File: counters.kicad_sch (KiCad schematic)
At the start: 21 parts, among them J10 Conn_01x10_Socket, J11 Conn_01x06_Socket, J12 Conn_01x10_Socket, J13 Conn_01x03_Socket, J8 Conn_01x10_Socket, J9 Conn_01x06_Socket, SW1 SW_Push, SW2 SW_Push

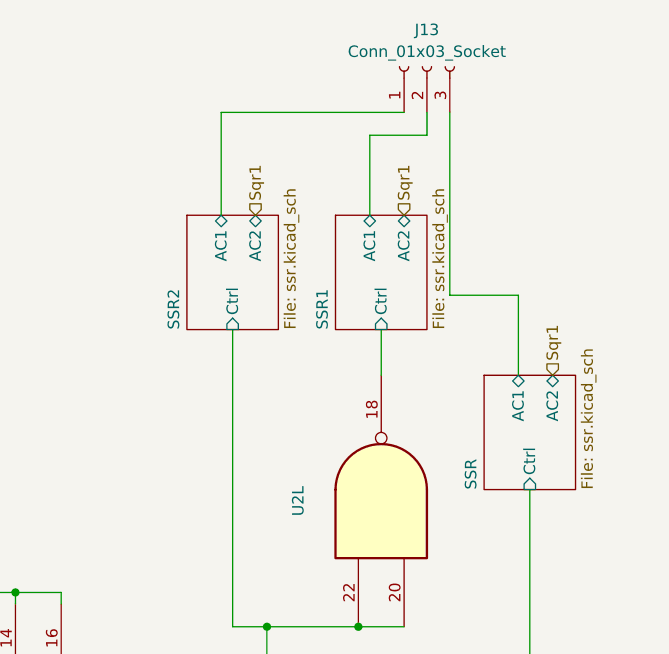
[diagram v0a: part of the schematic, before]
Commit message: switched to using SSR module
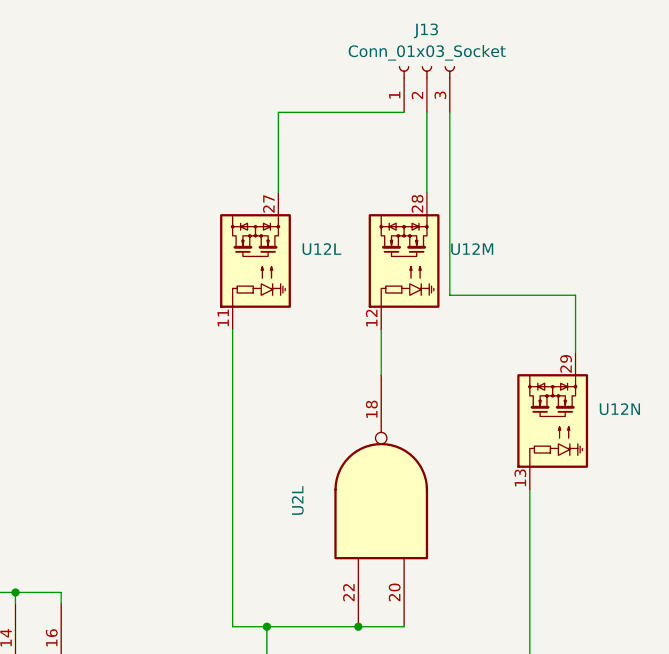
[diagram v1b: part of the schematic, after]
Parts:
- added U12: ~, symbol custom:SSR
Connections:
- net BCD_h1/Q0: now also U12.11
- net BCD_h1/Q1: now also U12.13
- net SSR/AC1: no longer names the net of J13.3 (Pin_3)
- net SSR/AC1: now also U12.29
- net SSR1/AC1: no longer names the net of J13.2 (Pin_2)
- net SSR1/AC1: now also U12.28
- net SSR1/Ctrl: no longer names the net of U2.18
- net SSR1/Ctrl: now also U12.12
- net SSR2/AC1: no longer names the net of J13.1 (Pin_1)
- net SSR2/AC1: now also U12.27
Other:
- removed sheet SSR
- removed sheet SSR1
- removed sheet SSR2

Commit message: added LCSC part numbers
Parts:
- C30, C31, C32, C33, C34, C35, C36: LCSC Part # (none) -> C57112
- R13, R15: LCSC Part # (none) -> C25804
- R14, R16: LCSC Part # (none) -> C21190
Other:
- sheet relays_m1 ports: added none; removed Sqr1
- sheet relays_s1 ports: added none; removed Sqr1

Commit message: switched clock to bjt astable multivibrator
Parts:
- U1: now not fitted
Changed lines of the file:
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@@
 		(in_bom yes)
 		(on_board yes)
-		(dnp no)
+		(dnp yes)
 		(property "Reference" "U1"
 			(at 217.678 113.538 90)
@@
 		(in_bom yes)
 		(on_board yes)
-		(dnp no)
+		(dnp yes)
 		(property "Reference" "U1"
 			(at 51.816 114.1617 90)
@@
 		(in_bom yes)
 		(on_board yes)
-		(dnp no)
+		(dnp yes)
 		(property "Reference" "U1"
 			(at 135.128 114.1617 90)

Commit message: changed some components to lcsc parts
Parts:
- U1: now fitted
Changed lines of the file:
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@@
 		(in_bom yes)
 		(on_board yes)
-		(dnp yes)
+		(dnp no)
 		(property "Reference" "U1"
 			(at 217.678 113.538 90)
@@
 		(in_bom yes)
 		(on_board yes)
-		(dnp yes)
+		(dnp no)
 		(property "Reference" "U1"
 			(at 51.816 114.1617 90)
@@
 		(in_bom yes)
 		(on_board yes)
-		(dnp yes)
+		(dnp no)
 		(property "Reference" "U1"
 			(at 135.128 114.1617 90)

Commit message: added footprints for modules
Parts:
- U14: renamed from U1; footprint (none) -> custom:module_bdc_mpcie
- U15: renamed from U2; footprint (none) -> custom:module_bdc_mpcie
- U9: renamed from U12; footprint (none) -> custom:module_ssr
- renumbered C30 to C16, C31 to C17, C32 to C18, C33 to C19, C34 to C20, C35 to C21, C36 to C22

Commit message: added module for PSU
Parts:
- U3: renamed from U9; value ~ -> SSR
- U8: renamed from U14; value ~ -> bin-to-dec; LCSC Part # (none) -> C185937
- U9: renamed from U15; value ~ -> bin-to-dec; LCSC Part # (none) -> C185937
- renumbered R13 to R14, R14 to R15, R15 to R16, R16 to R17
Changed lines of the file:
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@@
 		(on_board yes)
 		(dnp no)
-		(property "Reference" "U14"
+		(property "Reference" "U8"
 			(at 217.678 113.538 90)
 			(effects
@@
 			)
 		)
-		(property "Value" "~"
+		(property "Value" "bin-to-dec"
 			(at 219.202 115.316 90)
 			(effects
@@
 			)
 		)
-		(property "LCSC Part #" ""
+		(property "LCSC Part #" "C185937"
 			(at 228.6 96.52 90)
 			(effects
@@
 			(project "transistor-clock"
 				(path "/ce10d5bc-995e-4952-aa76-0a08f713a0f2/2c36a9e9-de42-4705-9ad4-94f4cc168e2f"
-					(reference "U14")
+					(reference "U8")
 					(unit 13)
 				)
@@
 		(dnp no)
 		(fields_autoplaced yes)
-		(property "Reference" "U9"
+		(property "Reference" "U3"
 			(at 281.432 78.7978 90)
 			(effects
@@
 			)
 		)
-		(property "Value" "~"
+		(property "Value" "SSR"
 			(at 281.432 81.2221 90)
 			(effects
@@
 			(project "transistor-clock"
 				(path "/ce10d5bc-995e-4952-aa76-0a08f713a0f2/2c36a9e9-de42-4705-9ad4-94f4cc168e2f"
-					(reference "U9")
+					(reference "U3")
 					(unit 14)
 				)
@@
 		(dnp no)
 		(fields_autoplaced yes)
-		(property "Reference" "U15"
+		(property "Reference" "U9"
 			(at 76.189 133.0155 0)
 			(effects
@@
 			)
 		)
-		(property "Value" "~"
+		(property "Value" "bin-to-dec"
 			(at 76.189 135.4398 0)
 			(effects
@@
 			)
 		)
-		(property "LCSC Part #" ""
+		(property "LCSC Part #" "C185937"
 			(at 63.5 135.89 0)
 			(effects
@@
 			(project "transistor-clock"
 				(path "/ce10d5bc-995e-4952-aa76-0a08f713a0f2/2c36a9e9-de42-4705-9ad4-94f4cc168e2f"
-					(reference "U15")
+					(reference "U9")
 					(unit 3)
 				)
@@
 		(on_board yes)
 		(dnp no)
-		(property "Reference" "R13"
+		(property "Reference" "R14"
 			(at 43.2605 138.43 90)
 			(effects
@@
 			(project "transistor-clock"
 				(path "/ce10d5bc-995e-4952-aa76-0a08f713a0f2/2c36a9e9-de42-4705-9ad4-94f4cc168e2f"
-					(reference "R13")
+					(reference "R14")
 					(unit 1)
 				)
@@
 		(dnp no)
 		(fields_autoplaced yes)
-		(property "Reference" "R14"
+		(property "Reference" "R15"
 			(at 36.322 151.1878 0)
 			(effects
@@
 			(project "transistor-clock"
 				(path "/ce10d5bc-995e-4952-aa76-0a08f713a0f2/2c36a9e9-de42-4705-9ad4-94f4cc168e2f"
-					(reference "R14")
+					(reference "R15")
 					(unit 1)
 				)
@@
 		(on_board yes)
 		(dnp no)
-		(property "Reference" "U15"
+		(property "Reference" "U9"
 			(at 90.424 114.046 90)
 			(effects
@@
 			)
 		)
-		(property "Value" "~"
+		(property "Value" "bin-to-dec"
 			(at 90.424 116.4703 90)
 			(effects
@@
 			)
 		)
-		(property "LCSC Part #" ""
+		(property "LCSC Part #" "C185937"
 			(at 101.6 96.52 90)
 			(effects
@@
 			(project "transistor-clock"
 				(path "/ce10d5bc-995e-4952-aa76-0a08f713a0f2/2c36a9e9-de42-4705-9ad4-94f4cc168e2f"
-					(reference "U15")
+					(reference "U9")
 					(unit 11)
 				)
@@
 		(dnp no)
 		(fields_autoplaced yes)
-		(property "Reference" "R16"
+		(property "Reference" "R17"
 			(at 82.042 168.9678 0)
 			(effects
@@
 			(project "transistor-clock"
 				(path "/ce10d5bc-995e-4952-aa76-0a08f713a0f2/2c36a9e9-de42-4705-9ad4-94f4cc168e2f"
-					(reference "R16")
+					(reference "R17")
 					(unit 1)
 				)
@@
 		(dnp no)
 		(fields_autoplaced yes)
-		(property "Reference" "U9"
+		(property "Reference" "U3"
 			(at 248.412 61.0178 90)
 			(effects
@@
 			)
 		)
-		(property "Value" "~"
+		(property "Value" "SSR"
 			(at 248.412 63.4421 90)
 			(effects
@@
 			(project "transistor-clock"
 				(path "/ce10d5bc-995e-4952-aa76-0a08f713a0f2/2c36a9e9-de42-4705-9ad4-94f4cc168e2f"
-					(reference "U9")
+					(reference "U3")
 					(unit 12)
 				)
@@
 		(dnp no)
 		(fields_autoplaced yes)
-		(property "Reference" "U9"
+		(property "Reference" "U3"
 			(at 264.922 61.0178 90)
 			(effects
@@
 			)
 		)
-		(property "Value" "~"
+		(property "Value" "SSR"
 			(at 264.922 63.4421 90)
 			(effects
@@
 			(project "transistor-clock"
 				(path "/ce10d5bc-995e-4952-aa76-0a08f713a0f2/2c36a9e9-de42-4705-9ad4-94f4cc168e2f"
-					(reference "U9")
+					(reference "U3")
 					(unit 13)
 				)
@@
 		(on_board yes)
 		(dnp no)
-		(property "Reference" "U14"
+		(property "Reference" "U8"
 			(at 51.816 114.1617 90)
 			(effects
@@
 			)
 		)
-		(property "Value" "~"
+		(property "Value" "bin-to-dec"
 			(at 51.816 116.586 90)
 			(effects
@@
 			)
 		)
-		(property "LCSC Part #" ""
+		(property "LCSC Part #" "C185937"
 			(at 60.96 97.79 90)
 			(effects
@@
 			(project "transistor-clock"
 				(path "/ce10d5bc-995e-4952-aa76-0a08f713a0f2/2c36a9e9-de42-4705-9ad4-94f4cc168e2f"
-					(reference "U14")
+					(reference "U8")
 					(unit 10)
 				)
@@
 		(dnp no)
 		(fields_autoplaced yes)
-		(property "Reference" "U15"
+		(property "Reference" "U9"
 			(at 121.909 150.7955 0)
 			(effects
@@
 			)
 		)
-		(property "Value" "~"
+		(property "Value" "bin-to-dec"
 			(at 121.909 153.2198 0)
 			(effects
@@
 			)
 		)
-		(property "LCSC Part #" ""
+		(property "LCSC Part #" "C185937"
 			(at 106.68 153.67 0)
 			(effects
@@
 			(project "transistor-clock"
 				(path "/ce10d5bc-995e-4952-aa76-0a08f713a0f2/2c36a9e9-de42-4705-9ad4-94f4cc168e2f"
-					(reference "U15")
+					(reference "U9")
 					(unit 8)
 				)
@@
 		(on_board yes)
 		(dnp no)
-		(property "Reference" "U15"
+		(property "Reference" "U9"
 			(at 173.736 114.1617 90)
 			(effects
@@
 			)
 		)
-		(property "Value" "~"
+		(property "Value" "bin-to-dec"
 			(at 173.736 116.586 90)
 			(effects
@@
 			)
 		)
-		(property "LCSC Part #" ""
+		(property "LCSC Part #" "C185937"
 			(at 185.42 96.52 90)
 			(effects
@@
 			(project "transistor-clock"
 				(path "/ce10d5bc-995e-4952-aa76-0a08f713a0f2/2c36a9e9-de42-4705-9ad4-94f4cc168e2f"
-					(reference "U15")
+					(reference "U9")
 					(unit 13)
 				)
@@
 		(on_board yes)
 		(dnp no)
-		(property "Reference" "U14"
+		(property "Reference" "U8"
 			(at 135.128 114.1617 90)
 			(effects
@@
 			)
 		)
-		(property "Value" "~"
+		(property "Value" "bin-to-dec"
 			(at 135.128 116.586 90)
 			(effects
@@
 			)
 		)
-		(property "LCSC Part #" ""
+		(property "LCSC Part #" "C185937"
 			(at 146.05 96.52 90)
 			(effects
@@
 			(project "transistor-clock"
 				(path "/ce10d5bc-995e-4952-aa76-0a08f713a0f2/2c36a9e9-de42-4705-9ad4-94f4cc168e2f"
-					(reference "U14")
+					(reference "U8")
 					(unit 11)
 				)
@@
 		(dnp no)
 		(fields_autoplaced yes)
-		(property "Reference" "U15"
+		(property "Reference" "U9"
 			(at 263.652 87.6988 90)
 			(effects
@@
 			)
 		)
-		(property "Value" "~"
+		(property "Value" "bin-to-dec"
 			(at 263.652 90.1231 90)
 			(effects
@@
 			)
 		)
-		(property "LCSC Part #" ""
+		(property "LCSC Part #" "C185937"
 			(at 251.46 104.14 0)
 			(effects
@@
 			(project "transistor-clock"
 				(path "/ce10d5bc-995e-4952-aa76-0a08f713a0f2/2c36a9e9-de42-4705-9ad4-94f4cc168e2f"
-					(reference "U15")
+					(reference "U9")
 					(unit 12)
 				)
@@
 		(on_board yes)
 		(dnp no)
-		(property "Reference" "R15"
+		(property "Reference" "R16"
 			(at 88.9805 156.21 90)
 			(effects
@@
 			(project "transistor-clock"
 				(path "/ce10d5bc-995e-4952-aa76-0a08f713a0f2/2c36a9e9-de42-4705-9ad4-94f4cc168e2f"
-					(reference "R15")
+					(reference "R16")
 					(unit 1)
 				)
